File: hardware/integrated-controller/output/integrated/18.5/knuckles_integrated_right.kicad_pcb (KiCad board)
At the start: 4 copper layers, 130.3 x 107.9 mm, 106 parts, among them J1 TYPE-C-31-M-12, J2 S2B-PH-SM4-TB(LF)(SN), J3 SM04B-SRSS-TB(LF)(SN), J5 SWD pogo interface, J6 External 10k NTC pads, Q1 AO3401A, Q2 2N7002, Q3 2N7002, SW1 SSSS811101, SW2 SKRPANE010, U1 MDBT50Q-1MV2, U2 BQ25186DLHR, U3 TPS63031DSKR, U4 USBLC6-2SC6

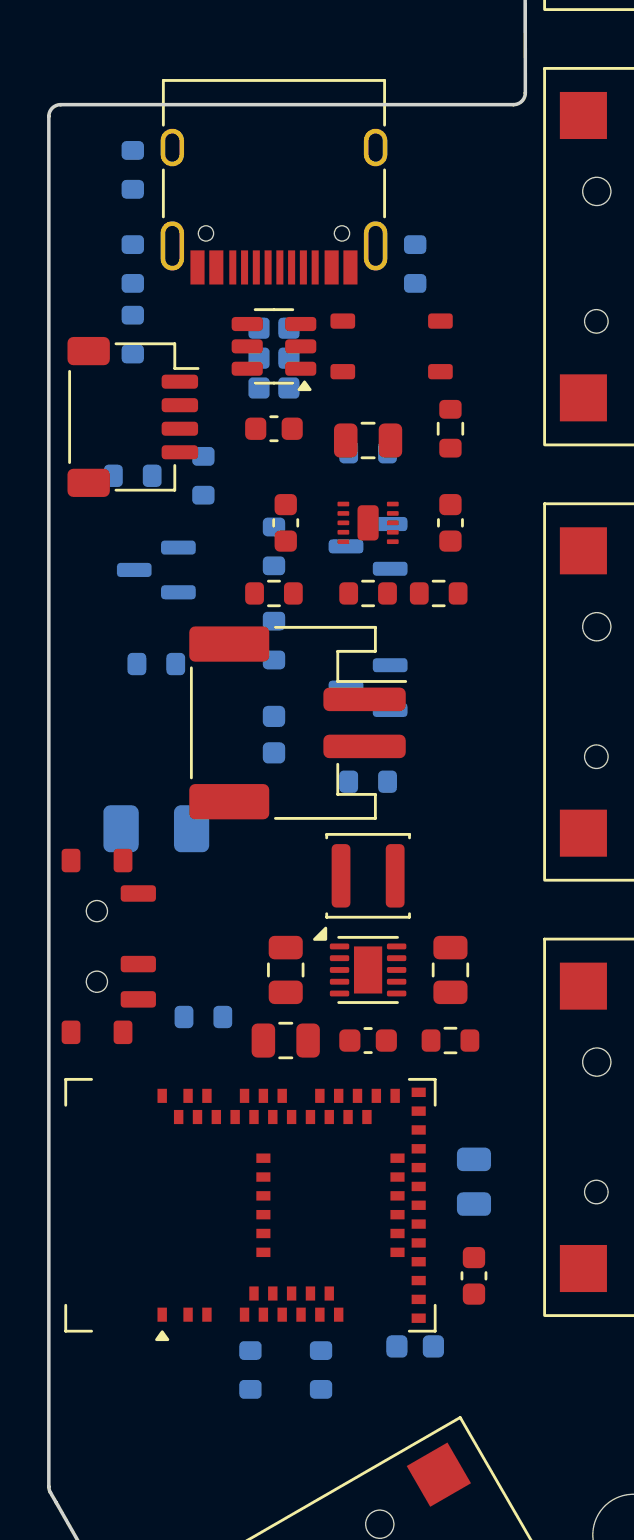
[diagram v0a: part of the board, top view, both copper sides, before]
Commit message: Route and validate integrated keyboard variants
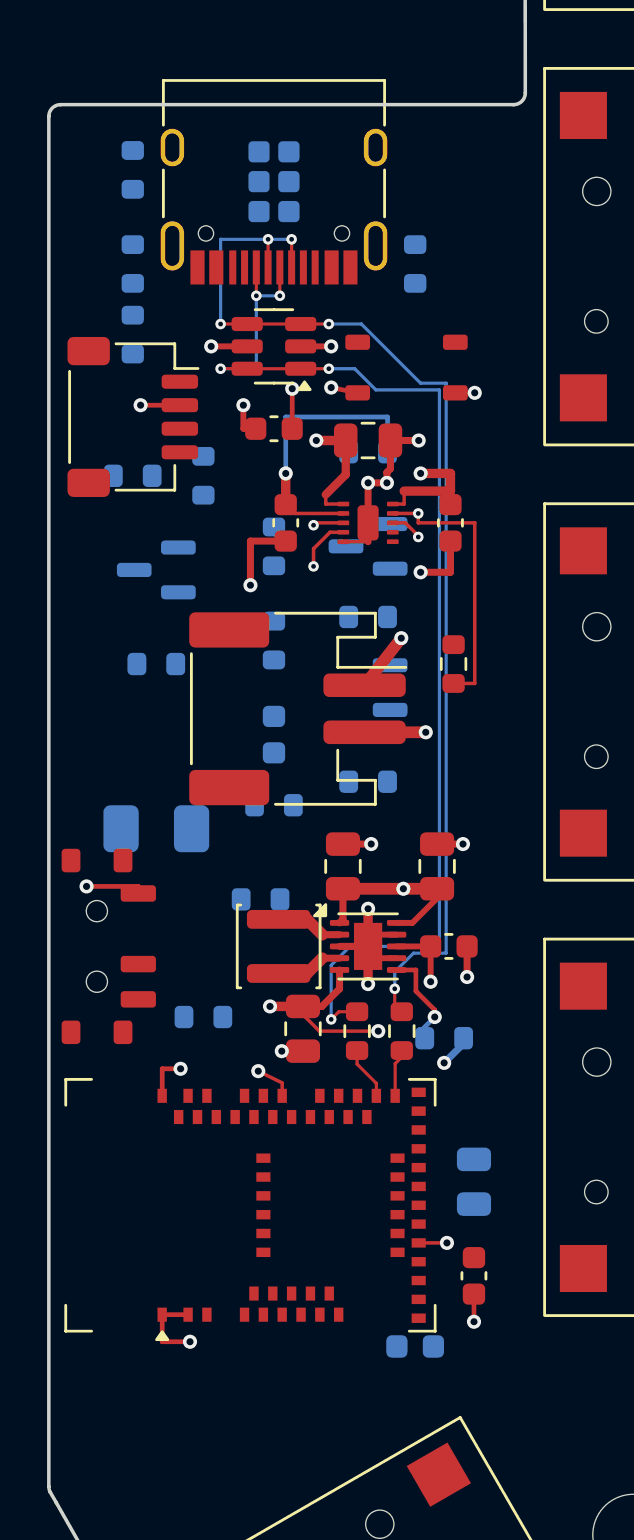
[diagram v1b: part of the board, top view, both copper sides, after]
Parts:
- L1: value 1.5uH SWPA3015S1R5MT -> 1.5uH SWPA3015S1R5NT
- R13, R7, R8, R9: moved to B.Cu
- R18, R19: moved to F.Cu
- moved R19 15.8 mm to (115.0, 93.6)
- moved R7 15.0 mm to (109.0, 88.0), turned to 180 degrees
- moved R18 14.5 mm to (113.1, 93.6)
- moved R6 10.0 mm to (117.2, 78.0)
- moved C11 9.80 mm to (116.5, 86.6), turned to 90 degrees
- moved R9 9.00 mm to (109.6, 84.0), turned to 180 degrees
- moved J5 7.50 mm to (109.6, 57.5)
- moved C4 7.00 mm to (117.1, 72.0)
- moved C5 7.00 mm to (110.1, 72.0)
- moved C8 6.75 mm to (110.8, 93.5)
- moved C9 5.27 mm to (117.0, 90.0)
- moved C10 5.03 mm to (112.5, 86.6), turned to 90 degrees
- moved L1 4.84 mm to (109.8, 90.0), turned to 90 degrees
- moved SW2 1.10 mm to (115.2, 65.4)
- moved R8 1.00 mm to (113.6, 76.0), turned to 180 degrees
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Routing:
- net USB_DP: track 0.00 -> 49.8 mm, vias 0 -> 5
- net SYS: track 0.00 -> 49.0 mm, vias 0 -> 4
- net USB_DN: track 0.00 -> 48.2 mm, vias 0 -> 5
- net GND: track 0.00 -> 43.4 mm, vias 0 -> 22
- net VBAT: track 0.00 -> 26.6 mm, vias 0 -> 2
- net VBUS: track 0.00 -> 18.2 mm, vias 0 -> 3
- net CHG_INT_N: track 0.00 -> 11.6 mm, vias 0 -> 1
- net +3V3: track 0.00 -> 8.06 mm, vias 0 -> 1
- net REG_EN: track 0.00 -> 4.23 mm, vias 0 -> 1
- net SW_L2: track 0.00 -> 2.86 mm
- net SW_L1: track 0.00 -> 2.86 mm
- net CHG_EN_N: track 0.00 -> 2.31 mm, vias 0 -> 1
- net USB_MCU_DP: track 0.00 -> 2.26 mm
- net USB_MCU_DN: track 0.00 -> 2.04 mm
- net TPS_SCL: track 0.00 -> 1.68 mm, vias 0 -> 1
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- added copper zone on In1.Cu, net GND
- added copper zone on In2.Cu, net GND
